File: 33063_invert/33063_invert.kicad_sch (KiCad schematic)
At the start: 14 parts, among them J1 Conn_01x02, J2 Conn_01x02, U1 33063

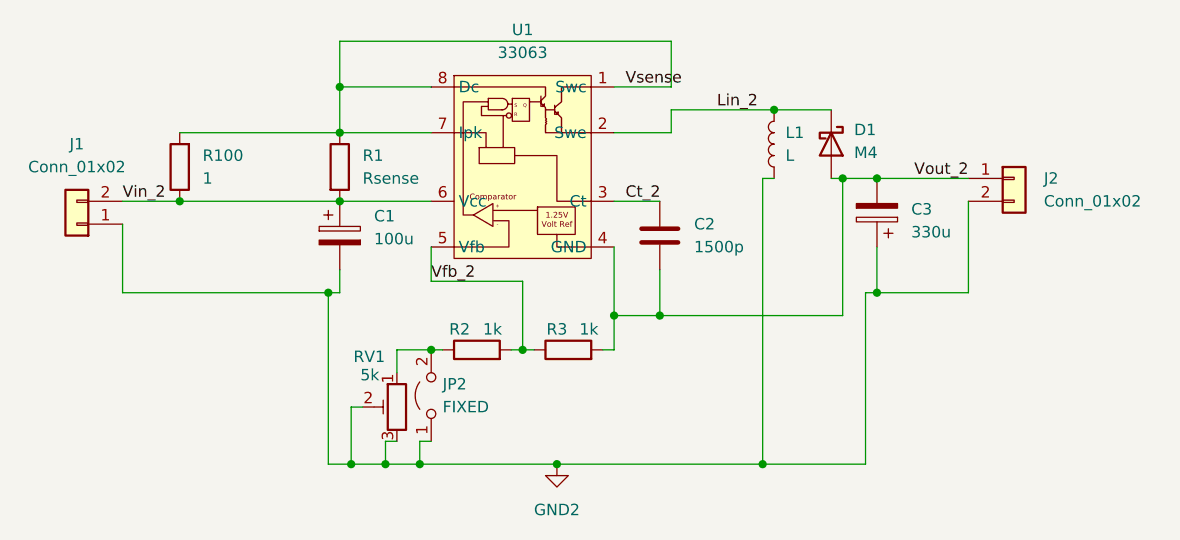
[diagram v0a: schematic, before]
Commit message: added DFN breakout changed trim pot type in 33063_boost, 33063_invert, r1283_power boards fixed error in 33063_boost board (move trim pot to higher side of voltage divider)
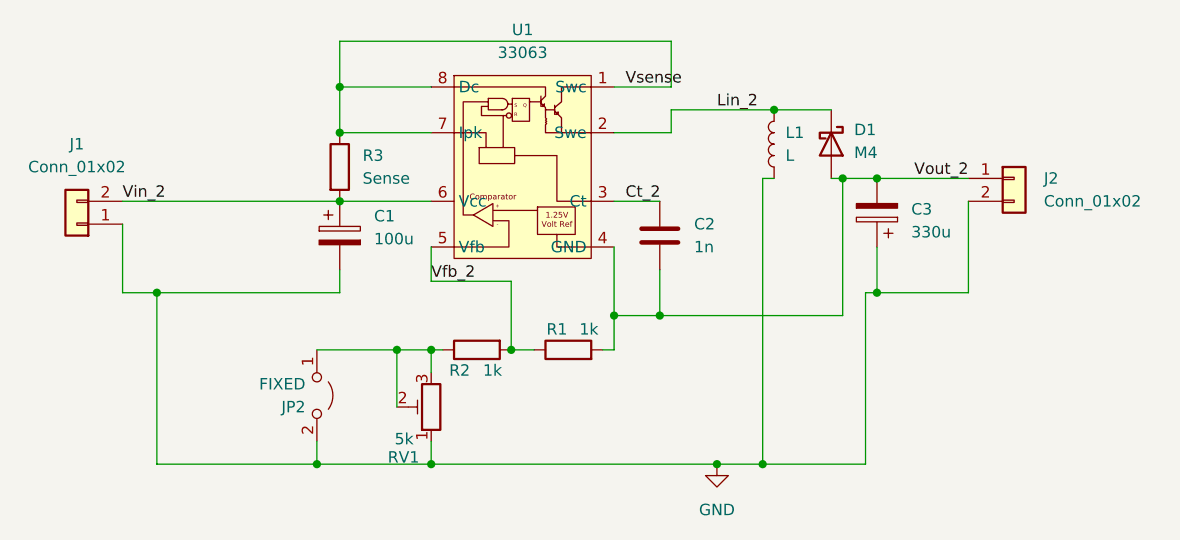
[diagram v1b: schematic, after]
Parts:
- removed R100: 1, misc:0805_5mm, symbol Device:R
- C2: value 1500p -> 1n
- R3: renamed from R1; value Rsense -> Sense; footprint Resistor_SMD:R_2512_6332Metric_Pad1.40x3.35mm_HandSolder -> Resistor_SMD:R_0805_2012Metric_Pad1.20x1.40mm_HandSolder
- RV1: footprint misc:trim_pot -> Potentiometer_THT:Potentiometer_Bourns_3296W_Vertical
- renumbered R3 to R1
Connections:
- net GND: now reaches JP2.2 (B), RV1.1
- net GND: now also C1.2, C3.1, J1.1 (Pin_1), J2.2 (Pin_2), L1.1; no longer R2.1
- removed net GND2: C1.2, C3.1, J1.1 (Pin_1), J2.2 (Pin_2), JP2.1 (A), L1.1, RV1.2, RV1.3
- new net: JP2.1 (A), R2.1, RV1.2, RV1.3
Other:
- moved on the sheet: JP2, RV1
